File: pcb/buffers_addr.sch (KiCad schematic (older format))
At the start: 26 parts

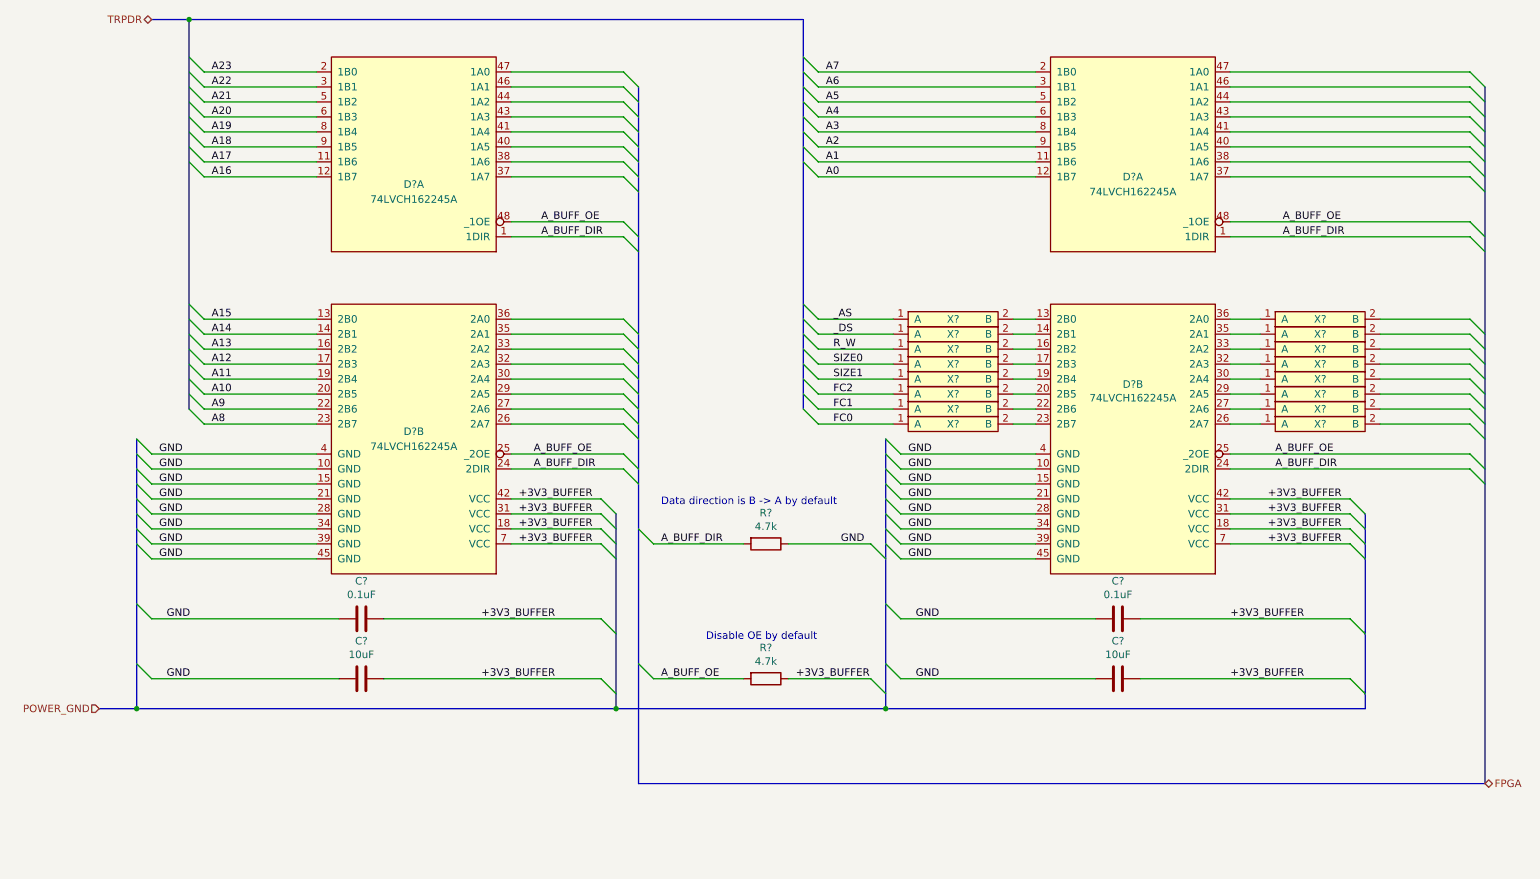
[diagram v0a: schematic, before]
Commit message: FPGA side labels added
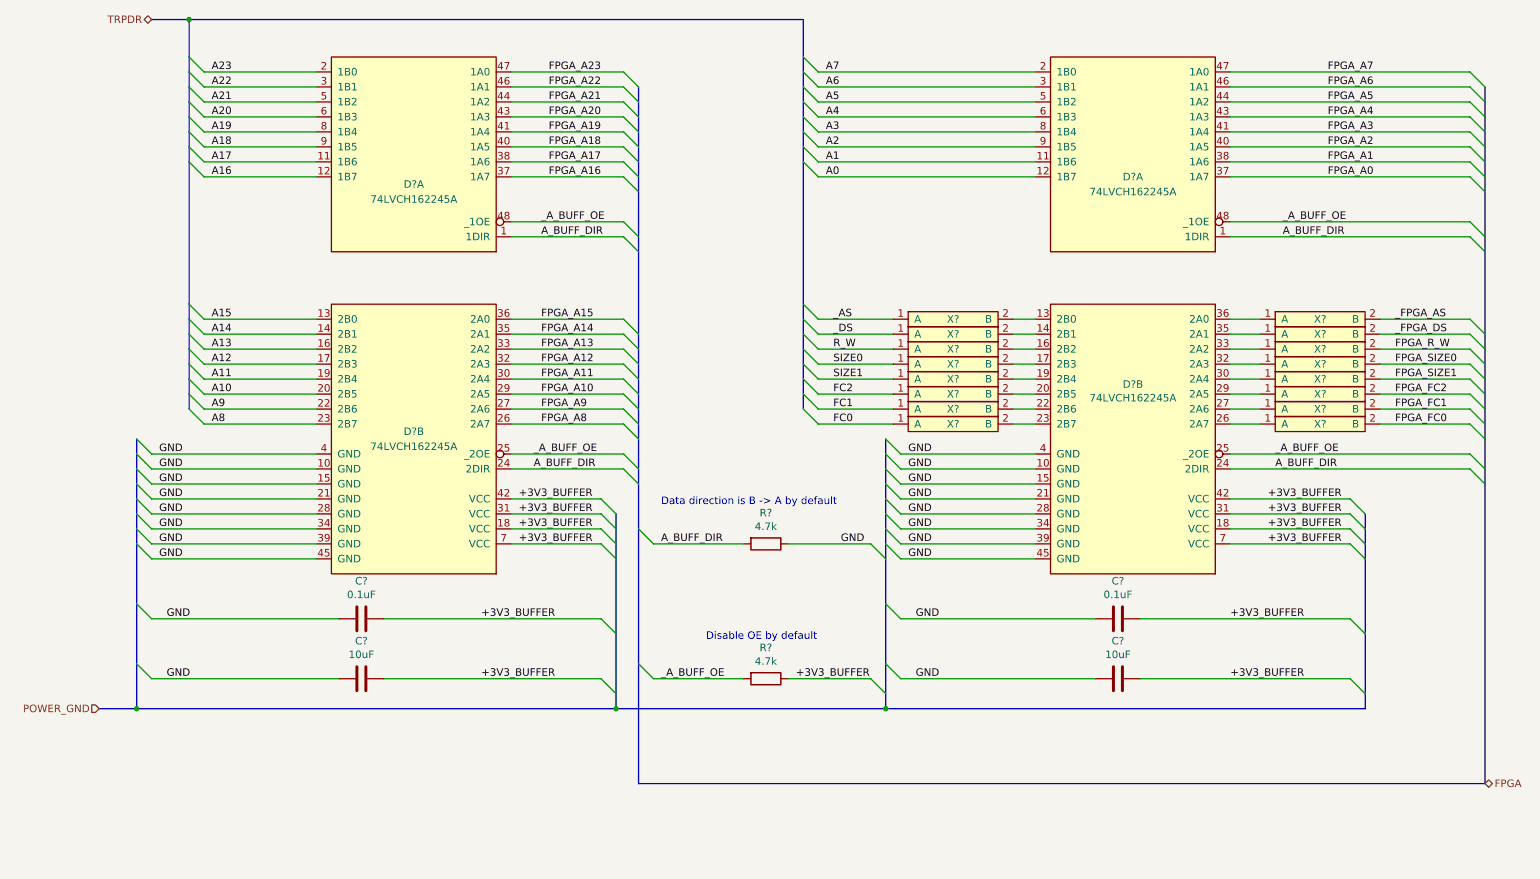
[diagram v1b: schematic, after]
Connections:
- net FPGA_A16: now reaches D?.37 (1A7)
- net FPGA_A17: now reaches D?.38 (1A6)
- net FPGA_A18: now reaches D?.40 (1A5)
- net FPGA_A19: now reaches D?.41 (1A4)
- net FPGA_A20: now reaches D?.43 (1A3)
- net FPGA_A21: now reaches D?.44 (1A2)
- net FPGA_A22: now reaches D?.46 (1A1)
- net FPGA_A23: now reaches D?.47 (1A0)
- net FPGA_A8: now reaches D?.26 (2A7)
- net FPGA_A9: now reaches D?.27 (2A6)
- net FPGA_A10: now reaches D?.29 (2A5)
- net FPGA_A11: now reaches D?.30 (2A4)
- net FPGA_A12: now reaches D?.32 (2A3)
- net FPGA_A13: now reaches D?.33 (2A2)
- net FPGA_A14: now reaches D?.35 (2A1)
- net FPGA_A15: now reaches D?.36 (2A0)
- net FPGA_A0: now reaches D?.37 (1A7)
- net FPGA_A1: now reaches D?.38 (1A6)
- net FPGA_A2: now reaches D?.40 (1A5)
- net FPGA_A3: now reaches D?.41 (1A4)
- net FPGA_A4: now reaches D?.43 (1A3)
- net FPGA_A5: now reaches D?.44 (1A2)
- net FPGA_A6: now reaches D?.46 (1A1)
- net FPGA_A7: now reaches D?.47 (1A0)
- net _FPGA_AS: now reaches X?.2 (B)
- net _FPGA_DS: now reaches X?.2 (B)
- net FPGA_R_W: now reaches X?.2 (B)
- net FPGA_SIZE0: now reaches X?.2 (B)
- net FPGA_SIZE1: now reaches X?.2 (B)
- net FPGA_FC2: now reaches X?.2 (B)
- net FPGA_FC1: now reaches X?.2 (B)
- net FPGA_FC0: now reaches X?.2 (B)
- net A_BUFF_OE renamed _A_BUFF_OE
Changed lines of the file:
@@
 GND
 Text Label 4100 2550 0    50   ~ 0
-A_BUFF_OE
+_A_BUFF_OE
 Text Label 4100 2650 0    50   ~ 0
 A_BUFF_DIR
 Text Label 4050 4100 0    50   ~ 0
-A_BUFF_OE
+_A_BUFF_OE
 Text Label 9050 2550 0    50   ~ 0
-A_BUFF_OE
+_A_BUFF_OE
 Text Label 9000 4100 0    50   ~ 0
-A_BUFF_OE
+_A_BUFF_OE
 Text Label 4050 4200 0    50   ~ 0
 A_BUFF_DIR
@@
 A_BUFF_DIR
 Text Label 4900 5600 0    50   ~ 0
-A_BUFF_OE
+_A_BUFF_OE
 Text Label 5800 5600 0    50   ~ 0
 +3V3_BUFFER
@@
 	10300 3900 9700 3900
 Wire Bus Line
+	1400 5800 4600 5800
+Text Label 4150 1550 0    50   ~ 0
+FPGA_A23
+Text Label 4150 1650 0    50   ~ 0
+FPGA_A22
+Text Label 4150 1750 0    50   ~ 0
+FPGA_A21
+Text Label 4150 1850 0    50   ~ 0
+FPGA_A20
+Text Label 4150 1950 0    50   ~ 0
+FPGA_A19
+Text Label 4150 2050 0    50   ~ 0
+FPGA_A18
+Text Label 4150 2150 0    50   ~ 0
+FPGA_A17
+Text Label 4150 2250 0    50   ~ 0
+FPGA_A16
+Text Label 4100 3200 0    50   ~ 0
+FPGA_A15
+Text Label 4100 3300 0    50   ~ 0
+FPGA_A14
+Text Label 4100 3400 0    50   ~ 0
+FPGA_A13
+Text Label 4100 3500 0    50   ~ 0
+FPGA_A12
+Text Label 4100 3600 0    50   ~ 0
+FPGA_A11
+Text Label 4100 3700 0    50   ~ 0
+FPGA_A10
+Text Label 4100 3800 0    50   ~ 0
+FPGA_A9
+Text Label 4100 3900 0    50   ~ 0
+FPGA_A8
+Text Label 9350 1550 0    50   ~ 0
+FPGA_A7
+Text Label 9350 1650 0    50   ~ 0
+FPGA_A6
+Text Label 9350 1750 0    50   ~ 0
+FPGA_A5
+Text Label 9350 1850 0    50   ~ 0
+FPGA_A4
+Text Label 9350 1950 0    50   ~ 0
+FPGA_A3
+Text Label 9350 2050 0    50   ~ 0
+FPGA_A2
+Text Label 9350 2150 0    50   ~ 0
+FPGA_A1
+Text Label 9350 2250 0    50   ~ 0
+FPGA_A0
+Text Label 9800 3200 0    50   ~ 0
+_FPGA_AS
+Text Label 9800 3300 0    50   ~ 0
+_FPGA_DS
+Text Label 9800 3400 0    50   ~ 0
+FPGA_R_W
+Text Label 9800 3500 0    50   ~ 0
+FPGA_SIZE0
+Text Label 9800 3600 0    50   ~ 0
+FPGA_SIZE1
+Text Label 9800 3700 0    50   ~ 0
+FPGA_FC2
+Text Label 9800 3800 0    50   ~ 0
+FPGA_FC1
+Text Label 9800 3900 0    50   ~ 0
+FPGA_FC0
+Wire Bus Line
 	4600 4500 4600 5800
 Wire Bus Line
@@
 Wire Bus Line
 	4750 1650 4750 6300
-Wire Bus Line
-	1400 5800 4600 5800
 $EndSCHEMATC

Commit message: Some work done on the whole project
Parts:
- removed C?: 10uF, symbol Device:C
- removed C? (x2): 0.1uF, symbol Device:C
- removed D?: 74LVCH162245A, symbol WM1200:74LVCH162245A
- added C5, C7: 0.1uF, symbol Device:C
- added C6: 10uF, symbol Device:C
- added unit 2 of U4
- gave numbers to parts that had none: 21
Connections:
- net +3V3_BUFFER: now also C5.2, C6.2, C7.2, U4.18 (VCC), U4.31 (VCC), U4.42 (VCC), U4.7 (VCC)
- net A_BUFF_DIR: now also U4.24 (2DIR)
- net GND: now also C5.1, C6.1, C7.1, U4.10 (GND), U4.15 (GND), U4.21 (GND), U4.28 (GND), U4.34 (GND), U4.39 (GND), U4.4 (GND), U4.45 (GND)
- net _A_BUFF_OE: now also U4.25 (_2OE)
- net at XT6.2 (B): now also U4.13 (2B0)
- net at XT7.2 (B): now also U4.14 (2B1)
- net at XT8.2 (B): now also U4.16 (2B2)
- net at XT9.2 (B): now also U4.17 (2B3)
- net at XT10.2 (B): now also U4.19 (2B4)
- net at XT11.2 (B): now also U4.20 (2B5)
- net at XT12.2 (B): now also U4.22 (2B6)
- net at XT13.2 (B): now also U4.23 (2B7)
- net at XT21.1 (A): now also U4.26 (2A7)
- net at XT20.1 (A): now also U4.27 (2A6)
- net at XT19.1 (A): now also U4.29 (2A5)
- net at XT18.1 (A): now also U4.30 (2A4)
- net at XT17.1 (A): now also U4.32 (2A3)
- net at XT16.1 (A): now also U4.33 (2A2)
- net at XT15.1 (A): now also U4.35 (2A1)
- net at XT14.1 (A): now also U4.36 (2A0)
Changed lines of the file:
@@
 $Descr A4 11693 8268
 encoding utf-8
-Sheet 9 11
+Sheet 8 11
 Title "WishMaster 1200"
 Date ""
@@
 $EndDescr
 $Comp
-L WM1200:74LVCH162245A D?
+L WM1200:74LVCH162245A U3
 U 1 1 5E552A9B
 P 3250 2750
-F 0 "D?" H 3250 3200 50  0000 C CNN
+F 0 "U3" H 3250 3200 50  0000 C CNN
 F 1 "74LVCH162245A" H 3250 3100 50  0000 C CNN
 F 2 "" H 3250 2750 50  0001 C CNN
@@
 $EndComp
 $Comp
-L WM1200:74LVCH162245A D?
+L WM1200:74LVCH162245A U3
 U 2 1 5E556C63
 P 3250 4900
-F 0 "D?" H 3250 5850 50  0000 C CNN
+F 0 "U3" H 3250 5850 50  0000 C CNN
 F 1 "74LVCH162245A" H 3250 5750 50  0000 C CNN
 F 2 "" H 3250 4900 50  0001 C CNN
@@
 $EndComp
 $Comp
-L WM1200:74LVCH162245A D?
+L WM1200:74LVCH162245A U4
 U 1 1 5E5582DD
 P 8050 2750
-F 0 "D?" H 8050 3250 50  0000 C CNN
+F 0 "U4" H 8050 3250 50  0000 C CNN
 F 1 "74LVCH162245A" H 8050 3150 50  0000 C CNN
 F 2 "" H 8050 2750 50  0001 C CNN
@@
 $EndComp
 $Comp
-L WM1200:74LVCH162245A D?
-U 2 1 5E55BDDA
+L WM1200:74LVCH162245A U4
+U 2 1 5E91F421
 P 8050 4900
-F 0 "D?" H 8050 6165 50  0000 C CNN
+F 0 "U4" H 8050 6165 50  0000 C CNN
 F 1 "74LVCH162245A" H 8050 6074 50  0000 C CNN
 F 2 "" H 8050 4900 50  0001 C CNN
@@
 	9500 4700 8700 4700
 $Comp
-L Device:C C?
-U 1 1 5E78F0E1
+L Device:C C6
+U 1 1 5E91F422
 P 2900 5600
-F 0 "C?" V 3152 5600 50  0000 C CNN
+F 0 "C6" V 3152 5600 50  0000 C CNN
 F 1 "10uF" V 3061 5600 50  0000 C CNN
 F 2 "" H 2938 5450 50  0001 C CNN
@@
 $EndComp
 $Comp
-L Device:C C?
-U 1 1 5E78FE60
+L Device:C C5
+U 1 1 5E91F424
 P 2900 5200
-F 0 "C?" V 3152 5200 50  0000 C CNN
+F 0 "C5" V 3152 5200 50  0000 C CNN
 F 1 "0.1uF" V 3061 5200 50  0000 C CNN
 F 2 "" H 2938 5050 50  0001 C CNN
@@
 $EndComp
 $Comp
-L Device:C C?
+L Device:C C8
 U 1 1 5E79CB26
 P 7950 5600
-F 0 "C?" V 8202 5600 50  0000 C CNN
+F 0 "C8" V 8202 5600 50  0000 C CNN
 F 1 "10uF" V 8111 5600 50  0000 C CNN
 F 2 "" H 7988 5450 50  0001 C CNN
@@
 $EndComp
 $Comp
-L Device:C C?
-U 1 1 5E79CB2C
+L Device:C C7
+U 1 1 5E91F427
 P 7950 5200
-F 0 "C?" V 8202 5200 50  0000 C CNN
+F 0 "C7" V 8202 5200 50  0000 C CNN
 F 1 "0.1uF" V 8111 5200 50  0000 C CNN
 F 2 "" H 7988 5050 50  0001 C CNN
@@
 FC0
 $Comp
-L WM1200:testpoint_cutline X?
+L WM1200:testpoint_cutline XT6
 U 1 1 5E57C393
 P 6850 3250
-F 0 "X?" H 6850 3300 50  0000 C CNN
+F 0 "XT6" H 6850 3300 50  0000 C CNN
 F 1 "testpoint_cutline" H 6850 3400 50  0001 C CNN
 F 2 "" H 7000 3250 50  0001 C CNN
@@
 $EndComp
 $Comp
-L WM1200:testpoint_cutline X?
+L WM1200:testpoint_cutline XT7
 U 1 1 5E57D0C2
 P 6850 3350
-F 0 "X?" H 6850 3400 50  0000 C CNN
+F 0 "XT7" H 6850 3400 50  0000 C CNN
 F 1 "testpoint_cutline" H 6850 3500 50  0001 C CNN
 F 2 "" H 7000 3350 50  0001 C CNN
@@
 $EndComp
 $Comp
-L WM1200:testpoint_cutline X?
+L WM1200:testpoint_cutline XT8
 U 1 1 5E57DCF2
 P 6850 3450
-F 0 "X?" H 6850 3500 50  0000 C CNN
+F 0 "XT8" H 6850 3500 50  0000 C CNN
 F 1 "testpoint_cutline" H 6850 3600 50  0001 C CNN
 F 2 "" H 7000 3450 50  0001 C CNN
@@
 $EndComp
 $Comp
-L WM1200:testpoint_cutline X?
+L WM1200:testpoint_cutline XT9
 U 1 1 5E57E315
 P 6850 3550
-F 0 "X?" H 6850 3600 50  0000 C CNN
+F 0 "XT9" H 6850 3600 50  0000 C CNN
 F 1 "testpoint_cutline" H 6850 3700 50  0001 C CNN
 F 2 "" H 7000 3550 50  0001 C CNN
@@
 $EndComp
 $Comp
-L WM1200:testpoint_cutline X?
+L WM1200:testpoint_cutline XT10
 U 1 1 5E57E966
 P 6850 3650
-F 0 "X?" H 6850 3700 50  0000 C CNN
+F 0 "XT10" H 6850 3700 50  0000 C CNN
 F 1 "testpoint_cutline" H 6850 3800 50  0001 C CNN
 F 2 "" H 7000 3650 50  0001 C CNN
@@
 $EndComp
 $Comp
-L WM1200:testpoint_cutline X?
+L WM1200:testpoint_cutline XT11
 U 1 1 5E57EE80
 P 6850 3750
-F 0 "X?" H 6850 3800 50  0000 C CNN
+F 0 "XT11" H 6850 3800 50  0000 C CNN
 F 1 "testpoint_cutline" H 6850 3900 50  0001 C CNN
 F 2 "" H 7000 3750 50  0001 C CNN
@@
 $EndComp
 $Comp
-L WM1200:testpoint_cutline X?
+L WM1200:testpoint_cutline XT12
 U 1 1 5E57F468
 P 6850 3850
-F 0 "X?" H 6850 3900 50  0000 C CNN
+F 0 "XT12" H 6850 3900 50  0000 C CNN
 F 1 "testpoint_cutline" H 6850 4000 50  0001 C CNN
 F 2 "" H 7000 3850 50  0001 C CNN
@@
 $EndComp
 $Comp
-L WM1200:testpoint_cutline X?
+L WM1200:testpoint_cutline XT13
 U 1 1 5E57FB7E
 P 6850 3950
-F 0 "X?" H 6850 4000 50  0000 C CNN
+F 0 "XT13" H 6850 4000 50  0000 C CNN
 F 1 "testpoint_cutline" H 6850 4100 50  0001 C CNN
 F 2 "" H 7000 3950 50  0001 C CNN
@@
 P 5600 4700
 AR Path="/5E5B89F7/5E91CEB5" Ref="R?"  Part="1"
-AR Path="/5E78104B/5E91CEB5" Ref="R?"  Part="1"
-F 0 "R?" V 5393 4700 50  0000 C CNN
+AR Path="/5E78104B/5E91CEB5" Ref="R15"  Part="1"
+F 0 "R15" V 5393 4700 50  0000 C CNN
 F 1 "4.7k" V 5484 4700 50  0000 C CNN
 F 2 "" V 5530 4700 50  0001 C CNN
@@
 P 5600 5600
 AR Path="/5E5B89F7/5E91CEBB" Ref="R?"  Part="1"
-AR Path="/5E78104B/5E91CEBB" Ref="R?"  Part="1"
-F 0 "R?" V 5393 5600 50  0000 C CNN
+AR Path="/5E78104B/5E91CEBB" Ref="R16"  Part="1"
+F 0 "R16" V 5393 5600 50  0000 C CNN
 F 1 "4.7k" V 5484 5600 50  0000 C CNN
 F 2 "" V 5530 5600 50  0001 C CNN
@@
 	4750 6300 10400 6300
 $Comp
-L WM1200:testpoint_cutline X?
+L WM1200:testpoint_cutline XT14
 U 1 1 5EA42E26
 P 9300 3250
-F 0 "X?" H 9300 3300 50  0000 C CNN
+F 0 "XT14" H 9300 3300 50  0000 C CNN
 F 1 "testpoint_cutline" H 9300 3400 50  0001 C CNN
 F 2 "" H 9450 3250 50  0001 C CNN
@@
 $EndComp
 $Comp
-L WM1200:testpoint_cutline X?
+L WM1200:testpoint_cutline XT15
 U 1 1 5EA42E2C
 P 9300 3350
-F 0 "X?" H 9300 3400 50  0000 C CNN
+F 0 "XT15" H 9300 3400 50  0000 C CNN
 F 1 "testpoint_cutline" H 9300 3500 50  0001 C CNN
 F 2 "" H 9450 3350 50  0001 C CNN
@@
 $EndComp
 $Comp
-L WM1200:testpoint_cutline X?
+L WM1200:testpoint_cutline XT16
 U 1 1 5EA42E32
 P 9300 3450
-F 0 "X?" H 9300 3500 50  0000 C CNN
+F 0 "XT16" H 9300 3500 50  0000 C CNN
 F 1 "testpoint_cutline" H 9300 3600 50  0001 C CNN
 F 2 "" H 9450 3450 50  0001 C CNN
@@
 $EndComp
 $Comp
-L WM1200:testpoint_cutline X?
+L WM1200:testpoint_cutline XT17
 U 1 1 5EA42E38
 P 9300 3550
-F 0 "X?" H 9300 3600 50  0000 C CNN
+F 0 "XT17" H 9300 3600 50  0000 C CNN
 F 1 "testpoint_cutline" H 9300 3700 50  0001 C CNN
 F 2 "" H 9450 3550 50  0001 C CNN
@@
 $EndComp
 $Comp
-L WM1200:testpoint_cutline X?
+L WM1200:testpoint_cutline XT18
 U 1 1 5EA42E3E
 P 9300 3650
-F 0 "X?" H 9300 3700 50  0000 C CNN
+F 0 "XT18" H 9300 3700 50  0000 C CNN
 F 1 "testpoint_cutline" H 9300 3800 50  0001 C CNN
 F 2 "" H 9450 3650 50  0001 C CNN
@@
 $EndComp
 $Comp
-L WM1200:testpoint_cutline X?
+L WM1200:testpoint_cutline XT19
 U 1 1 5EA42E44
 P 9300 3750
-F 0 "X?" H 9300 3800 50  0000 C CNN
+F 0 "XT19" H 9300 3800 50  0000 C CNN
 F 1 "testpoint_cutline" H 9300 3900 50  0001 C CNN
 F 2 "" H 9450 3750 50  0001 C CNN
@@
 $EndComp
 $Comp
-L WM1200:testpoint_cutline X?
+L WM1200:testpoint_cutline XT20
 U 1 1 5EA42E4A
 P 9300 3850
-F 0 "X?" H 9300 3900 50  0000 C CNN
+F 0 "XT20" H 9300 3900 50  0000 C CNN
 F 1 "testpoint_cutline" H 9300 4000 50  0001 C CNN
 F 2 "" H 9450 3850 50  0001 C CNN
@@
 $EndComp
 $Comp
-L WM1200:testpoint_cutline X?
+L WM1200:testpoint_cutline XT21
 U 1 1 5EA42E50
 P 9300 3950
-F 0 "X?" H 9300 4000 50  0000 C CNN
+F 0 "XT21" H 9300 4000 50  0000 C CNN
 F 1 "testpoint_cutline" H 9300 4100 50  0001 C CNN
 F 2 "" H 9450 3950 50  0001 C CNN
